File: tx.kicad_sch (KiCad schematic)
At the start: 54 parts, among them U1 ADF4158, U10 HMC431LP4, U12 PAT1220-3dB, U14 TQP5525, U15 SMA, U3 PAT1220-6dB, U36 SolderPad_1_Circle, U7 TLV172DCK

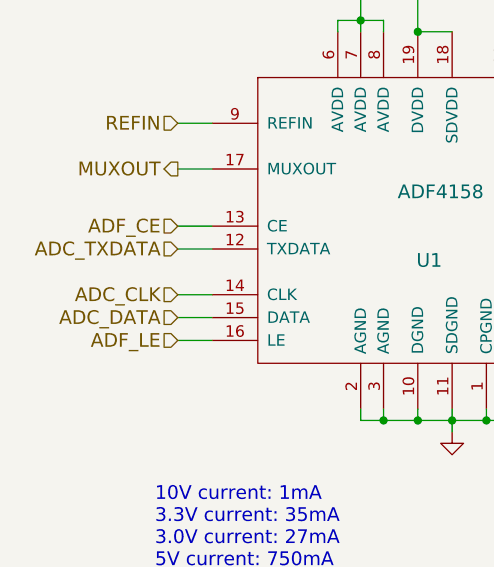
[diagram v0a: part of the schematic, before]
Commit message: 3 leds are added design is checked. Schematic pin name corrected
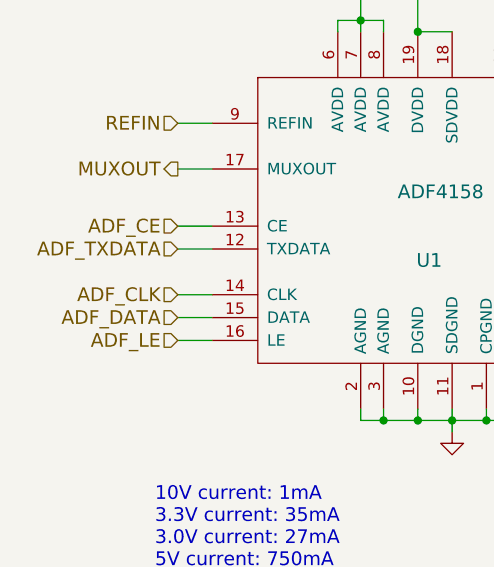
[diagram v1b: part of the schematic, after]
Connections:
- net ADC_CLK renamed ADF_CLK
- net ADC_DATA renamed ADF_DATA
- net ADC_TXDATA renamed ADF_TXDATA
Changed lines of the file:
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@@
 		)
 	)
-	(hierarchical_label "ADC_DATA"
+	(hierarchical_label "ADF_DATA"
 		(shape input)
 		(at 30.48 161.29 180)
@@
 		)
 	)
-	(hierarchical_label "ADC_TXDATA"
+	(hierarchical_label "ADF_TXDATA"
 		(shape input)
 		(at 30.48 153.67 180)
@@
 		)
 	)
-	(hierarchical_label "ADC_CLK"
+	(hierarchical_label "ADF_CLK"
 		(shape input)
 		(at 30.48 158.75 180)

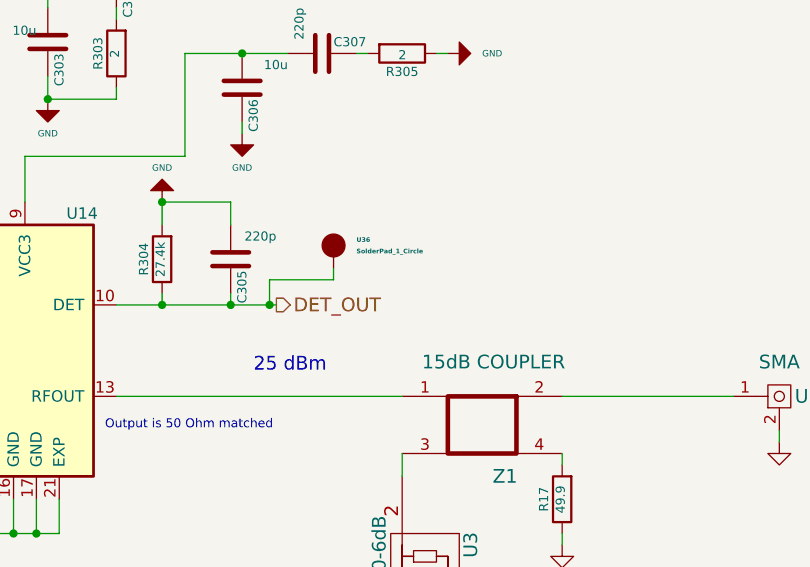
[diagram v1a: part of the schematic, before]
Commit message: Reset button is added. Detout is connected to an adc pin of fpga. Unused pad is deleted. Pins are check. Notes are added on pcb side. No problem related error drc excluded
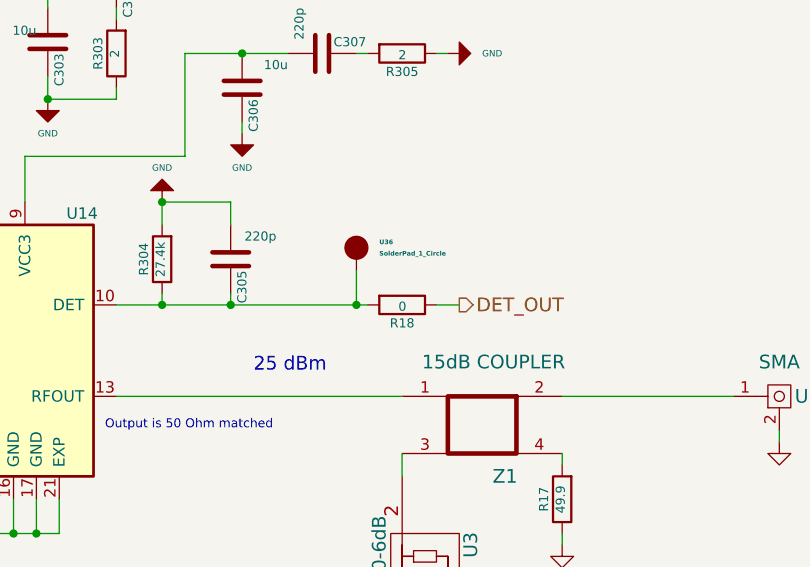
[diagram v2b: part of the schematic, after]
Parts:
- added R18: 0, Footprints:SMD_0402, symbol fmcw3-rescue:R
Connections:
- net DET_OUT: now also R18.1; no longer C305.1, R304.1, U14.10 (DET), U36.1
- new net: C305.1, R18.2, R304.1, U14.10 (DET), U36.1
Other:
- moved on the sheet: U36
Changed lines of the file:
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@@
 	)
 	(junction
-		(at 343.408 110.49)
+		(at 353.06 110.49)
 		(diameter 0)
 		(color 0 0 0 0)
@@
 	(wire
 		(pts
-			(xy 343.408 110.49) (xy 344.17 110.49)
-		)
-		(stroke
-			(width 0)
-			(type default)
-		)
-	)
-	(wire
-		(pts
 			(xy 243.84 146.05) (xy 243.84 153.67)
 		)
@@
 	(wire
 		(pts
-			(xy 343.408 110.49) (xy 343.408 107.696)
-		)
-		(stroke
-			(width 0)
-			(type default)
-		)
-	)
-	(wire
-		(pts
 			(xy 300.99 69.85) (xy 300.99 76.2)
 		)
@@
 	(wire
 		(pts
-			(xy 147.32 160.02) (xy 147.32 163.83)
+			(xy 361.95 110.49) (xy 364.49 110.49)
 		)
 		(stroke
@@
 	(wire
 		(pts
-			(xy 125.73 140.97) (xy 147.32 140.97)
+			(xy 147.32 160.02) (xy 147.32 163.83)
 		)
 		(stroke
@@
 	(wire
 		(pts
-			(xy 147.32 171.45) (xy 147.32 175.26)
+			(xy 125.73 140.97) (xy 147.32 140.97)
 		)
 		(stroke
@@
 	(wire
 		(pts
-			(xy 340.36 82.55) (xy 345.44 82.55)
+			(xy 147.32 171.45) (xy 147.32 175.26)
 		)
 		(stroke
@@
 	(wire
 		(pts
-			(xy 350.52 106.426) (xy 350.52 107.696)
+			(xy 340.36 82.55) (xy 345.44 82.55)
 		)
 		(stroke
@@
 	(wire
 		(pts
+			(xy 353.06 110.49) (xy 354.33 110.49)
+		)
+		(stroke
+			(width 0)
+			(type default)
+		)
+	)
+	(wire
+		(pts
 			(xy 189.23 115.57) (xy 191.77 115.57)
 		)
@@
 	(wire
 		(pts
-			(xy 339.09 110.49) (xy 343.408 110.49)
+			(xy 339.09 110.49) (xy 353.06 110.49)
 		)
 		(stroke
@@
 	(wire
 		(pts
-			(xy 343.408 107.696) (xy 350.52 107.696)
-		)
-		(stroke
-			(width 0)
-			(type default)
-		)
-	)
-	(wire
-		(pts
 			(xy 104.14 154.94) (xy 107.95 154.94)
 		)
@@
 	(wire
 		(pts
+			(xy 353.06 106.68) (xy 353.06 110.49)
+		)
+		(stroke
+			(width 0)
+			(type default)
+		)
+	)
+	(wire
+		(pts
 			(xy 83.82 149.86) (xy 87.63 149.86)
 		)
@@
 	(hierarchical_label "DET_OUT"
 		(shape output)
-		(at 344.17 110.49 0)
+		(at 364.49 110.49 0)
 		(effects
 			(font
@@
 	(symbol
 		(lib_id "SolderPad_1_Circle:SolderPad_1_Circle")
-		(at 350.52 103.886 270)
+		(at 353.06 104.14 270)
 		(unit 1)
 		(exclude_from_sim no)
@@
 		(fields_autoplaced yes)
 		(property "Reference" "U36"
-			(at 353.06 103.251 90)
+			(at 355.6 103.505 90)
 			(effects
 				(font
@@
 		)
 		(property "Value" "SolderPad_1_Circle"
-			(at 353.06 104.521 90)
+			(at 355.6 104.775 90)
 			(effects
 				(font
@@
 		)
 		(property "Footprint" "Footprints:SolderPad_1_1.5mm_SMD_Circle"
-			(at 350.52 103.886 0)
+			(at 353.06 104.14 0)
 			(effects
 				(font
@@
 		)
 		(property "Datasheet" ""
-			(at 350.52 103.886 0)
+			(at 353.06 104.14 0)
 			(effects
 				(font
@@
 		)
 		(property "Description" ""
-			(at 350.52 103.886 0)
+			(at 353.06 104.14 0)
 			(effects
 				(font
@@
 					(unit 1)
 				)
+			)
+		)
+	)
+	(symbol
+		(lib_id "fmcw3-rescue:R")
+		(at 358.14 110.49 270)
+		(unit 1)
+		(exclude_from_sim no)
+		(in_bom yes)
+		(on_board yes)
+		(dnp no)
+		(property "Reference" "R18"
+			(at 358.14 112.522 90)
+			(effects
+				(font
+					(size 1.016 1.016)
+				)
+			)
+		)
+		(property "Value" "0"
+			(at 358.1654 110.6678 90)
+			(effects
+				(font
+					(size 1.016 1.016)
+				)
+			)
+		)
+		(property "Footprint" "Footprints:SMD_0402"
+			(at 358.14 108.712 90)
+			(effects
+				(font
+					(size 0.762 0.762)
+				)
+				(hide yes)
+			)
+		)
+		(property "Datasheet" ""
+			(at 358.14 110.49 0)
+			(effects
+				(font
+					(size 0.762 0.762)
+				)
+			)
+		)
+		(property "Description" ""
+			(at 358.14 110.49 0)
+			(effects
+				(font
+					(size 1.27 1.27)
+				)
+			)
+		)
+		(pin "1"
+		)
+		(pin "2"
+		)
+		(instances
+			(project "fmcw3"
+				(path "/25ababa6-1178-4b22-9ad6-058222120a27/00000000-0000-0000-0000-000059396b94"
+					(reference "R18")
+					(unit 1)
+				)

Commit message: I have designed 0.17mm directional coupler and placed on pcb. Further improvements for better layout will be done
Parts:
- Z1: footprint Footprints:Directional_Coupler_15dB_0.23mm_v2 -> Footprints:Directional_Coupler_15dB_0.169mm_v2
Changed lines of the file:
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@@
 			)
 		)
-		(property "Footprint" "Footprints:Directional_Coupler_15dB_0.23mm_v2"
+		(property "Footprint" "Footprints:Directional_Coupler_15dB_0.169mm_v2"
 			(at 368.3 128.27 0)
 			(effects

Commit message: final corrections is done. Working!
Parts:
- C10: value 330n -> 2.2n
- C14: value 10n -> 220p
- C29: value 68p -> DNP
- R2: value DNP -> 3.3K
- R4: value 240 -> 1K
- R7: value 4.7k -> 0
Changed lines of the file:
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@@
 			)
 		)
-		(property "Value" "330n"
+		(property "Value" "2.2n"
 			(at 104.2924 150.749 0)
 			(effects
@@
 			)
 		)
-		(property "Value" "DNP"
+		(property "Value" "3.3K"
 			(at 91.4654 150.0378 90)
 			(effects
@@
 			)
 		)
-		(property "Value" "240"
+		(property "Value" "1K"
 			(at 108.1278 161.2646 90)
 			(effects
@@
 			)
 		)
-		(property "Value" "4.7k"
+		(property "Value" "0"
 			(at 180.3654 143.6878 90)
 			(effects
@@
 			)
 		)
-		(property "Value" "68p"
+		(property "Value" "DNP"
 			(at 189.3824 152.019 0)
 			(effects
@@
 			)
 		)
-		(property "Value" "10n"
+		(property "Value" "220p"
 			(at 125.8824 152.019 0)
 			(effects

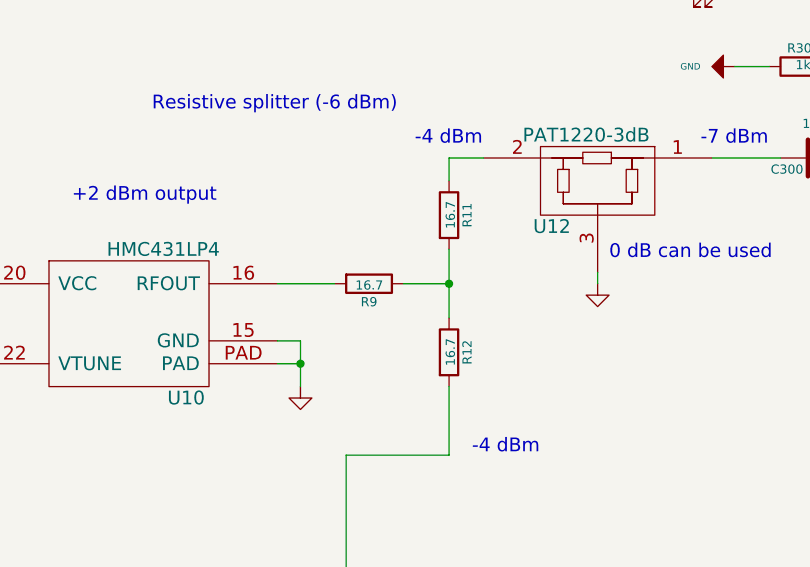
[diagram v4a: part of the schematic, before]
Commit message: clock buffer and txco source is changed. Clock is clipped sin and fanout says cmos square out but it is better anyways. Also traces are 50 ohm as well. Copper pours other minor thinks are changed as well
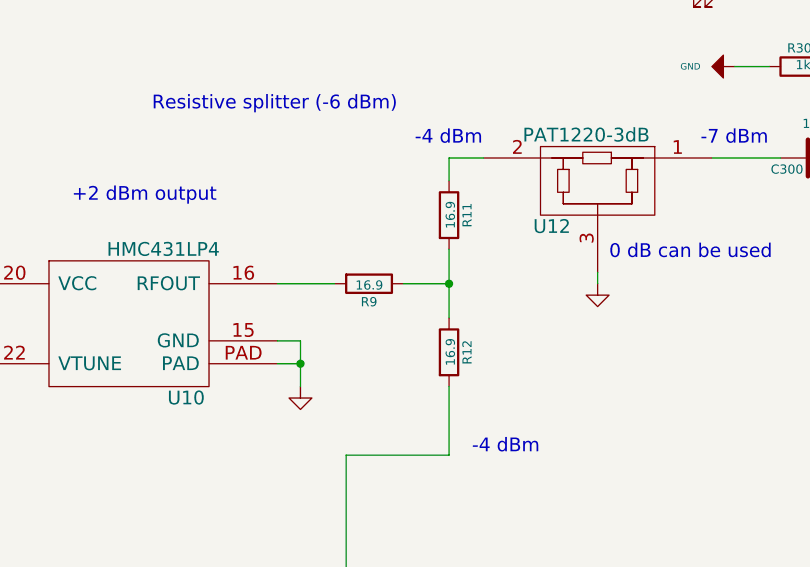
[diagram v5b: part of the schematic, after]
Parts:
- R11, R12, R9: value 16.7 -> 16.9
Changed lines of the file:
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@@
 			)
 		)
-		(property "Value" "16.7"
+		(property "Value" "16.9"
 			(at 234.9754 134.7978 90)
 			(effects
@@
 			)
 		)
-		(property "Value" "16.7"
+		(property "Value" "16.9"
 			(at 244.0178 126.9746 90)
 			(effects
@@
 			)
 		)
-		(property "Value" "16.7"
+		(property "Value" "16.9"
 			(at 244.0178 142.2146 90)
 			(effects

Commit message: hardware changes
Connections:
- net REFIN renamed ADF_CLK_REF
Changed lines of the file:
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@@
 		)
 	)
-	(hierarchical_label "REFIN"
+	(hierarchical_label "ADF_CLK_REF"
 		(shape input)
 		(at 30.48 139.7 180)

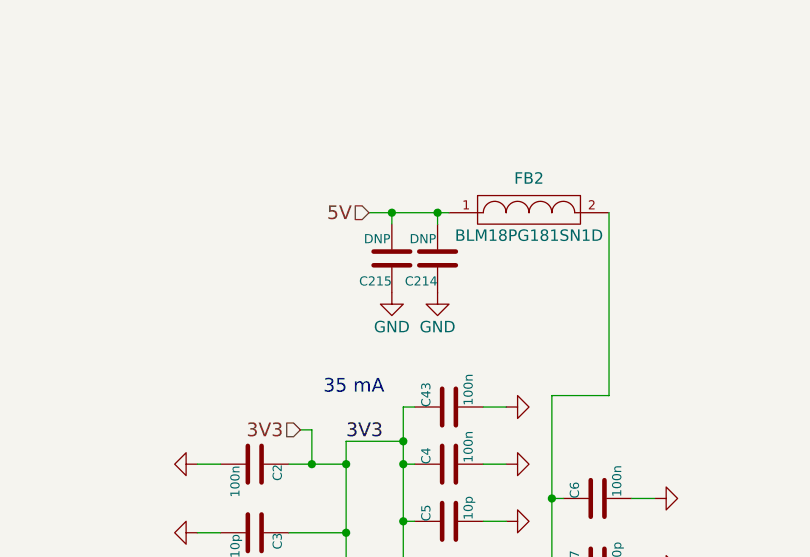
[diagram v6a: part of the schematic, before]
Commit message: DNP components are deleted
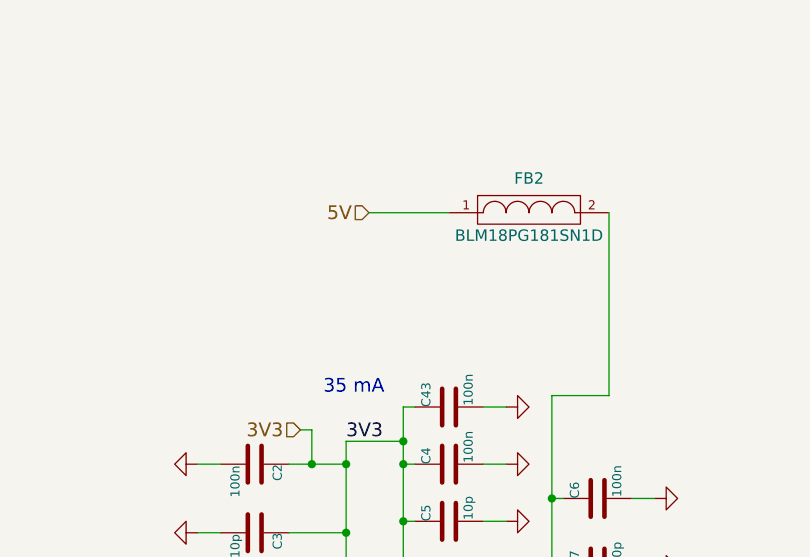
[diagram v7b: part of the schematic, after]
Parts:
- removed C214, C215: DNP, Footprints:SMD_0805, symbol fmcw3-rescue:C

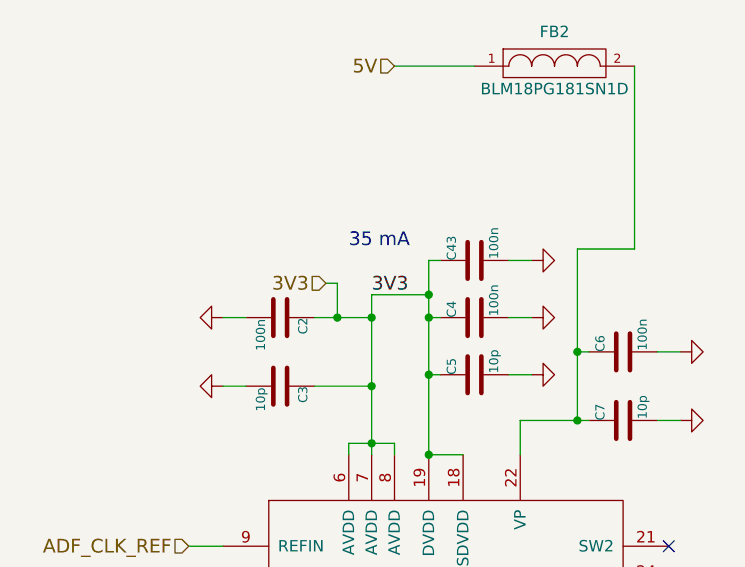
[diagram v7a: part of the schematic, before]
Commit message: pcb is checked dnp is deleted copper pours are checked
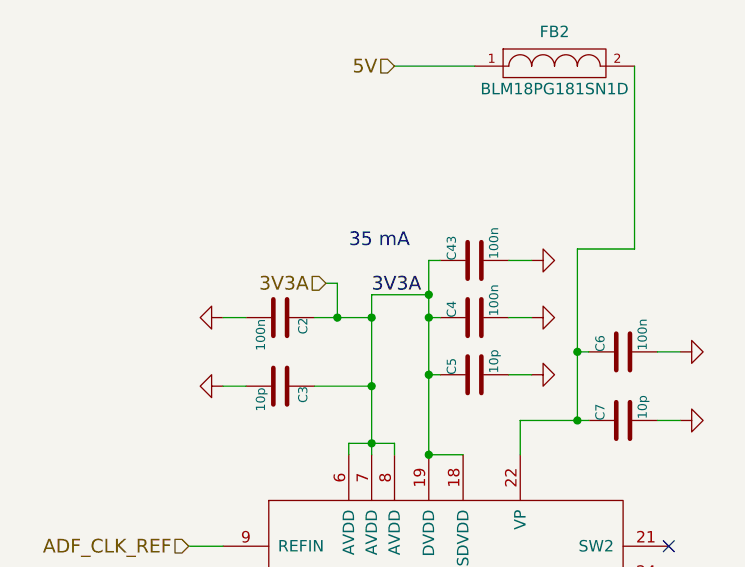
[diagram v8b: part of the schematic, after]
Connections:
- net 3V3 renamed 3V3A
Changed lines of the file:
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@@
 		)
 	)
-	(label "3V3"
+	(label "3V3A"
 		(at 50.8 111.76 0)
 		(effects
@@
 		)
 	)
-	(hierarchical_label "3V3"
+	(hierarchical_label "3V3A"
 		(shape input)
 		(at 45.72 110.49 180)
